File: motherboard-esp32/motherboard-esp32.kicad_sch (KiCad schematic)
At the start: 4 parts

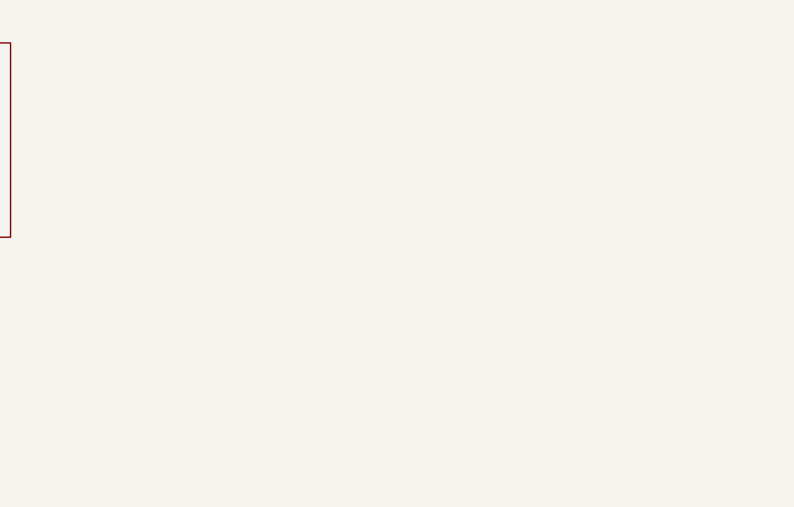
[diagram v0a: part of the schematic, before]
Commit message: adding leds
- need to add UVLO
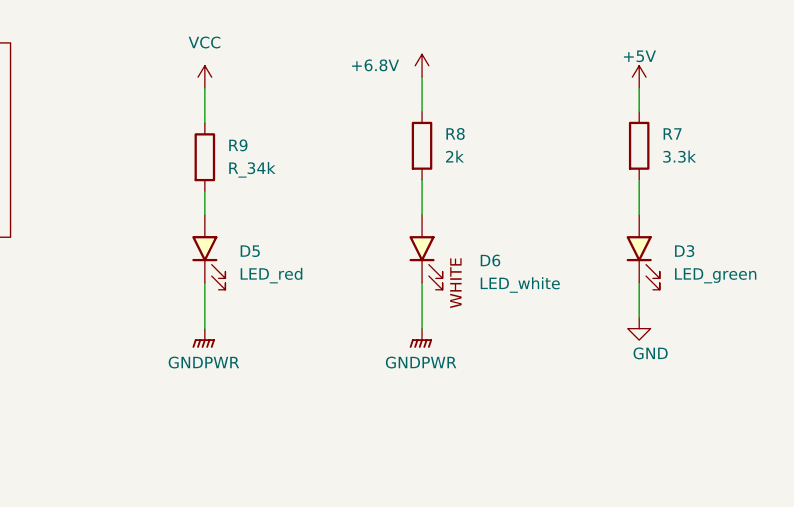
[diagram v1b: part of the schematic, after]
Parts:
- added D3: LED_green, bots:LED_0805_2012Metric, symbol bots:LED_green
- added D5: LED_red, bots:LED_1206MERGE0805, symbol bots:LED_red
- added D6: LED_white, bots:LED_0603_1608Metric, symbol bots:LED_white
- added R7: 3.3k, bots:R_0603_1608Metric, symbol bots:R_3.3k
- added R8: 2k, bots:R_0603_1608Metric, symbol bots:R_2k
- added R9: R_34k, bots:R_0603_1608Metric, symbol bots:R_34k
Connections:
- new net: D3.2 (A), R7.2
- new net: D6.2 (A), R8.2
- new net: D5.2 (A), R9.2
- new net +5V: R7.1
- new net +6.8V: R8.1
- new net GND: D3.1 (K)
- new net GNDPWR: D5.1 (K), D6.1 (K)
- new net VCC: R9.1

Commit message: 5V 5A version
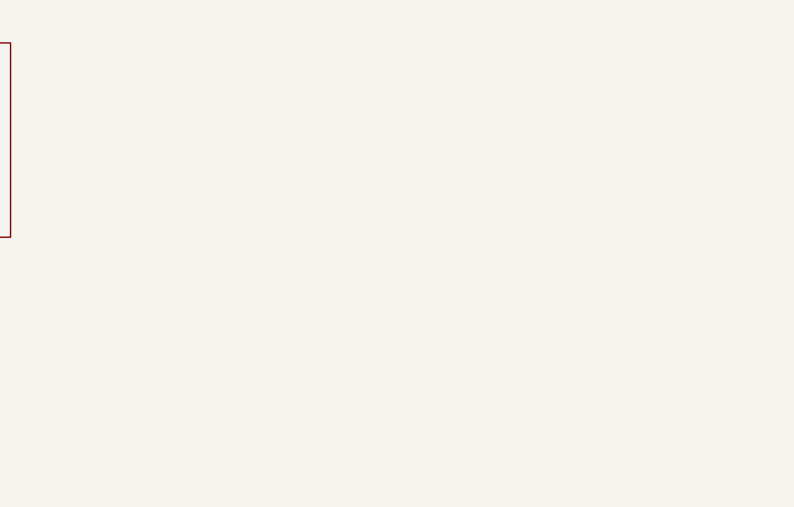
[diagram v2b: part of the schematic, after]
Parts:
- removed D3: LED_green, bots:LED_0805_2012Metric, symbol bots:LED_green
- removed D5: LED_red, bots:LED_1206MERGE0805, symbol bots:LED_red
- removed D6: LED_white, bots:LED_0603_1608Metric, symbol bots:LED_white
- removed R7: 3.3k, bots:R_0603_1608Metric, symbol bots:R_3.3k
- removed R8: 2k, bots:R_0603_1608Metric, symbol bots:R_2k
- removed R9: R_34k, bots:R_0603_1608Metric, symbol bots:R_34k
